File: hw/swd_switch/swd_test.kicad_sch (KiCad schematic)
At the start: 11 parts, among them J1 SWD_IN, J2 Conn_01x04, J3 SWD_PWR, J4 SWD_OUT, U1 SN74LVC2G66, U2 SN74LVC2G66, U3 SN74LVC2G66

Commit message: Added MPNs for SWD_Switch
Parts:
- J1, J4: DKPN (none) -> 609-3695-1-ND; MPN (none) -> 20021121-00010C4LF
- U1, U2, U3: DKPN (none) -> 296-13272-1-ND; MPN (none) -> SN74LVC2G66DCUR
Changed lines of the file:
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@@
-(kicad_sch (version 20210621) (generator eeschema)
+(kicad_sch (version 20211123) (generator eeschema)
   (paper "A4")
   (title_block
     (title "Debugotron SWD Switch")
-    (date "2021-11-14")
+    (date "2022-01-16")
     (rev "1.0")
     (company "Quesadillon LLC")
   )
-  (junction (at 218.44 114.3) (diameter 0) (color 0 0 0 0))
-  (junction (at 81.28 43.18) (diameter 0) (color 0 0 0 0))
-  (junction (at 88.9 114.3) (diameter 0) (color 0 0 0 0))
-  (junction (at 88.9 38.1) (diameter 0) (color 0 0 0 0))
+  (junction (at 88.9 38.1) (diameter 0) (color 0 0 0 0)
+  )
+  (junction (at 81.28 43.18) (diameter 0) (color 0 0 0 0)
+  )
+  (junction (at 218.44 114.3) (diameter 0) (color 0 0 0 0)
+  )
+  (junction (at 88.9 114.3) (diameter 0) (color 0 0 0 0)
+  )
   (wire (pts (xy 81.28 55.88) (xy 81.28 58.42))
     (stroke (width 0) (type default) (color 0 0 0 0))
@@
     )
     (property "Datasheet" "http://infocenter.arm.com/help/topic/com.arm.doc.ddi0314h/DDI0314H_coresight_components_trm.pdf" (id 3) (at 227.33 128.27 90)
+      (effects (font (size 1.27 1.27)) hide)
+    )
+    (property "DKPN" "609-3695-1-ND" (id 4) (at 218.44 96.52 0)
+      (effects (font (size 1.27 1.27)) hide)
+    )
+    (property "MPN" "20021121-00010C4LF" (id 5) (at 218.44 96.52 0)
       (effects (font (size 1.27 1.27)) hide)
     )
@@
       (effects (font (size 1.27 1.27)) hide)
     )
+    (property "DKPN" "296-13272-1-ND" (id 4) (at 147.32 93.98 0)
+      (effects (font (size 1.27 1.27)) hide)
+    )
+    (property "MPN" "SN74LVC2G66DCUR" (id 5) (at 147.32 93.98 0)
+      (effects (font (size 1.27 1.27)) hide)
+    )
     (pin "1")
     (pin "2")
@@
     )
     (property "Datasheet" "http://infocenter.arm.com/help/topic/com.arm.doc.ddi0314h/DDI0314H_coresight_components_trm.pdf" (id 3) (at 80.01 128.27 90)
+      (effects (font (size 1.27 1.27)) hide)
+    )
+    (property "DKPN" "609-3695-1-ND" (id 4) (at 88.9 96.52 0)
+      (effects (font (size 1.27 1.27)) hide)
+    )
+    (property "MPN" "20021121-00010C4LF" (id 5) (at 88.9 96.52 0)
       (effects (font (size 1.27 1.27)) hide)
     )
@@
       (effects (font (size 1.27 1.27)) hide)
     )
+    (property "DKPN" "296-13272-1-ND" (id 4) (at 147.32 58.42 0)
+      (effects (font (size 1.27 1.27)) hide)
+    )
+    (property "MPN" "SN74LVC2G66DCUR" (id 5) (at 147.32 58.42 0)
+      (effects (font (size 1.27 1.27)) hide)
+    )
     (pin "1")
     (pin "2")
@@
       (effects (font (size 1.27 1.27)) hide)
     )
+    (property "DKPN" "296-13272-1-ND" (id 4) (at 147.32 129.54 0)
+      (effects (font (size 1.27 1.27)) hide)
+    )
+    (property "MPN" "SN74LVC2G66DCUR" (id 5) (at 147.32 129.54 0)
+      (effects (font (size 1.27 1.27)) hide)
+    )

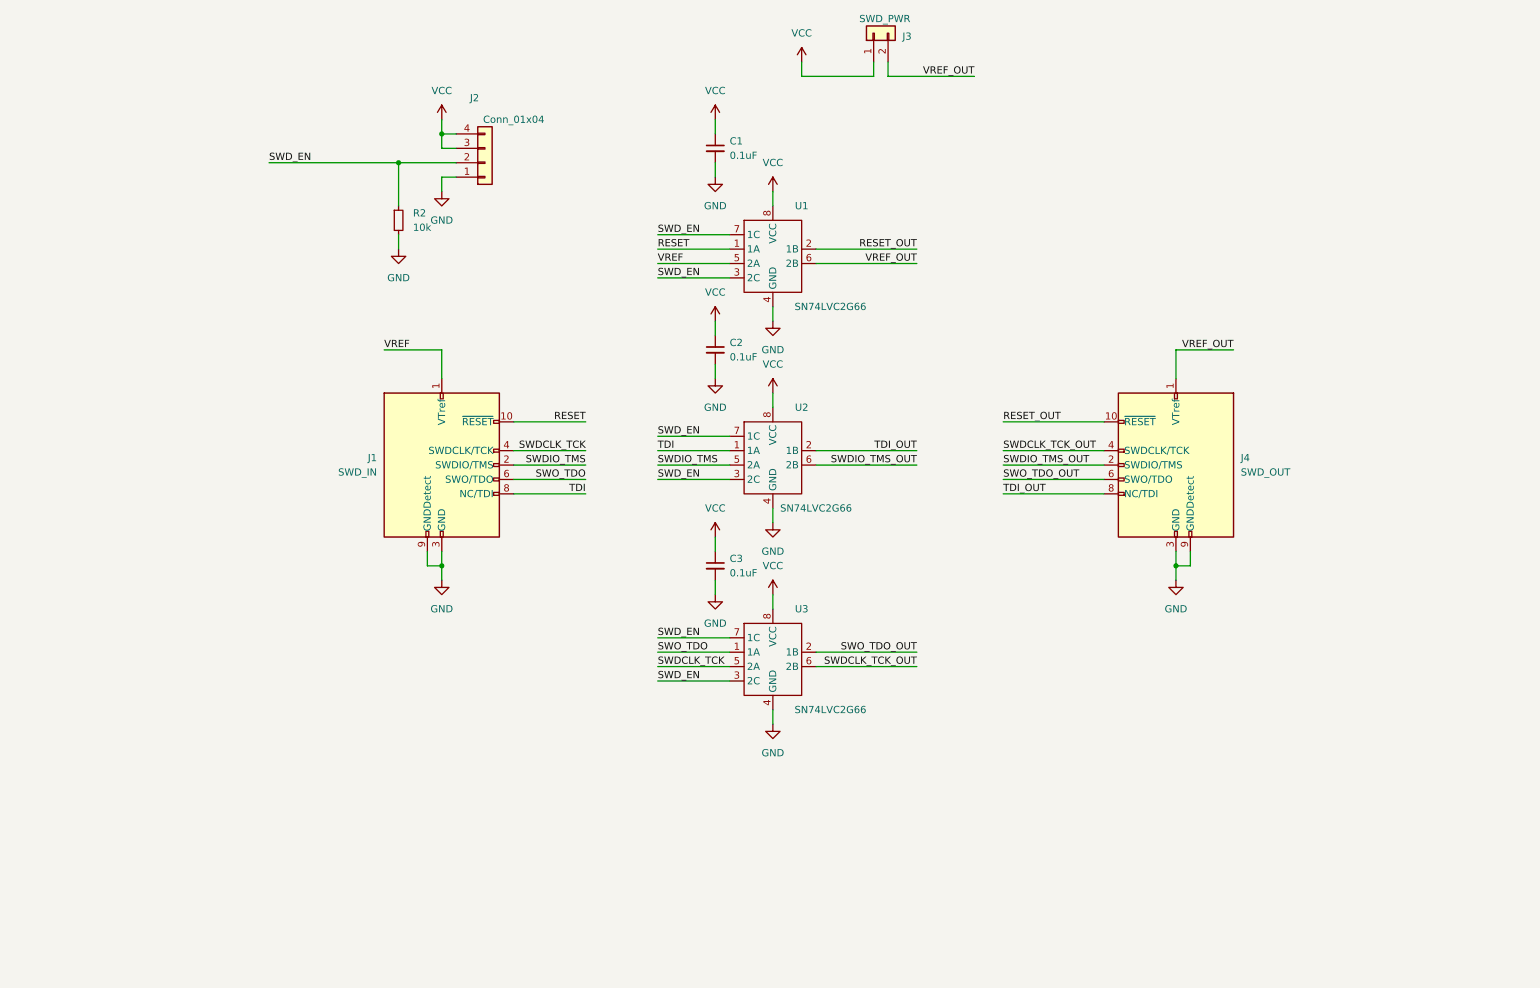
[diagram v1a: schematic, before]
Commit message: Updated debugotron v2.0 and ordered
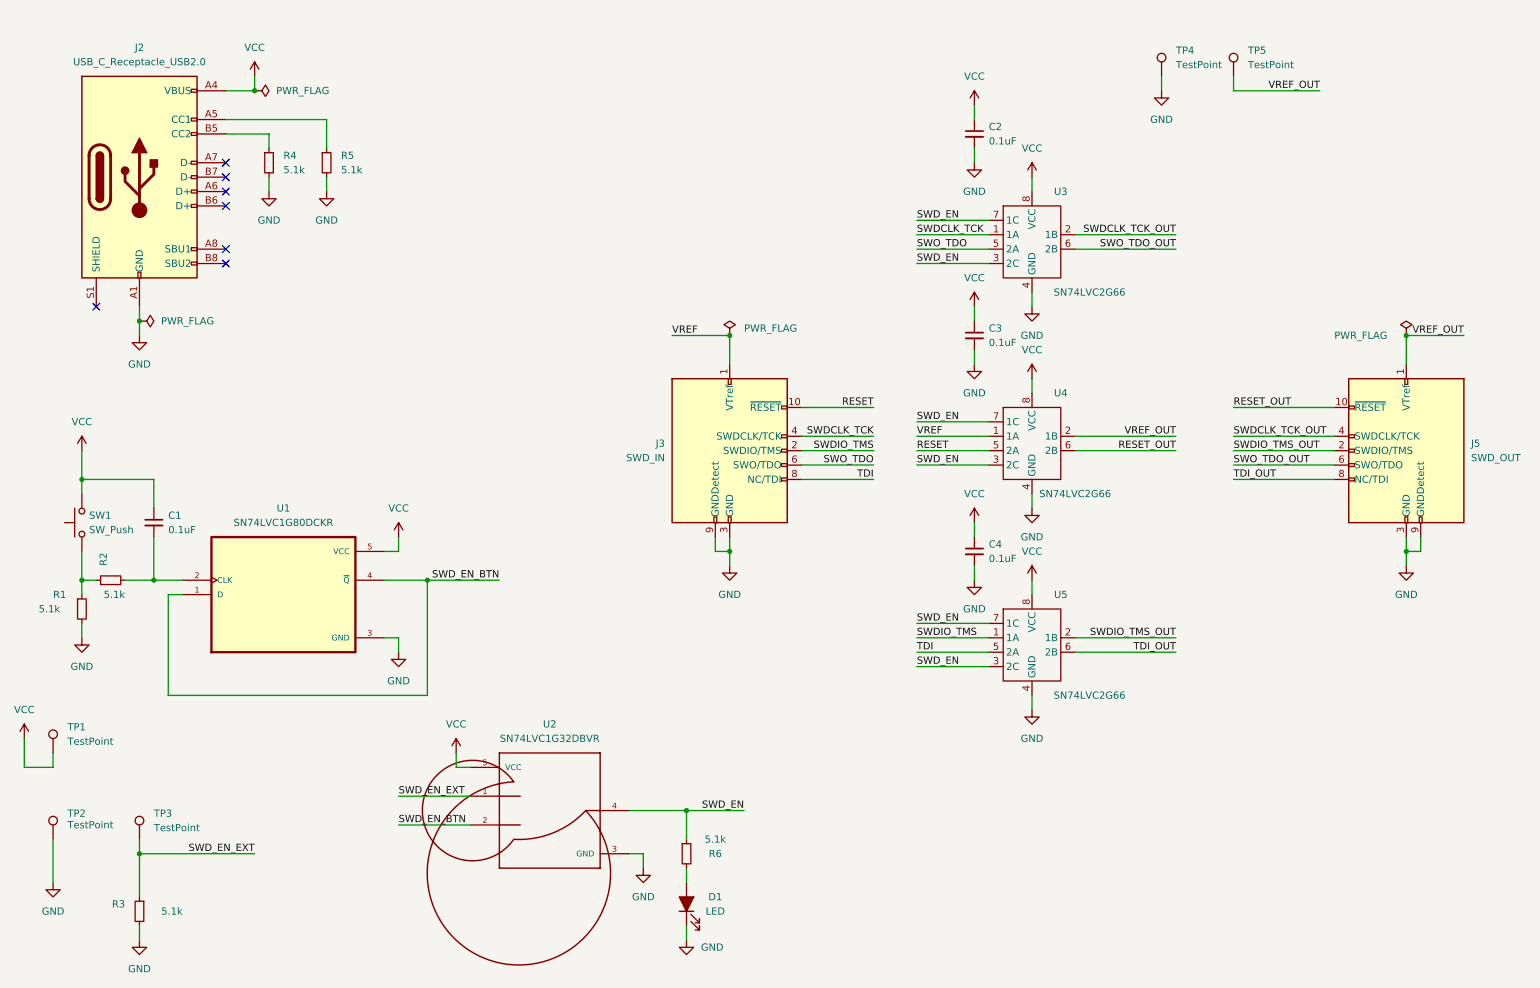
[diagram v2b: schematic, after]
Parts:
- removed J2: Conn_01x04, Connector_PinHeader_2.54mm:PinHeader_1x04_P2.54mm_Vertical, symbol Connector_Generic:Conn_01x04
- removed J3: SWD_PWR, Connector_PinHeader_2.54mm:PinHeader_1x02_P2.54mm_Vertical, symbol Connector_Generic:Conn_01x02
- added C1: 0.1uF, Capacitor_SMD:C_0402_1005Metric, symbol Device:C_Small
- added D1: LED, LED_SMD:LED_0603_1608Metric, symbol Device:LED_Filled
- added J2: USB_C_Receptacle_USB2.0, alvarop:USB4515-GF-A, symbol Connector:USB_C_Receptacle_USB2.0
- added R1, R2, R4, R5, R6: 5.1k, Resistor_SMD:R_0402_1005Metric, symbol Device:R_Small
- added SW1: SW_Push, alvarop:PTS636_G, symbol Switch:SW_Push
- added TP1, TP2, TP3, TP4, TP5: TestPoint, TestPoint:TestPoint_Pad_D3.0mm, symbol Connector:TestPoint
- added U1: SN74LVC1G80DCKR, snapeda:SOT65P210X110-5N, symbol snapeda:SN74LVC1G80DCKR
- added U2: SN74LVC1G32DBVR, snapeda:SOT95P280X145-5N, symbol snapeda:SN74LVC1G32DBVR
- J3: renamed from J1; footprint Connector_PinHeader_1.27mm:PinHeader_2x05_P1.27mm_Vertical_SMD -> snapeda:SAMTEC_FTSH-105-01-F-DV-P-TR_alt
- J5: renamed from J4; footprint Connector_PinHeader_1.27mm:PinHeader_2x05_P1.27mm_Vertical_SMD -> snapeda:SAMTEC_FTSH-105-01-F-DV-P-TR_alt
- R3: renamed from R2; value 10k -> 5.1k
- U3: renamed from U1; footprint alvaro:SN74LVC2G66-VSSOP -> alvarop:SN74LVC2G66-VSSOP
- U4: renamed from U2; footprint alvaro:SN74LVC2G66-VSSOP -> alvarop:SN74LVC2G66-VSSOP
- U5: renamed from U3; footprint alvaro:SN74LVC2G66-VSSOP -> alvarop:SN74LVC2G66-VSSOP
- renumbered C1 to C2, C2 to C3, C3 to C4
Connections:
- net GND: now also D1.1 (K), J2.A1 (GND), J2.A12 (GND), J2.B1 (GND), J2.B12 (GND), R1.2, R4.2, R5.2, TP2.1, TP4.1, U1.3 (GND), U2.3 (GND)
- net RESET: now also U4.5 (2A); no longer U3.1 (1A)
- net RESET_OUT: now also U4.6 (2B); no longer U3.2 (1B)
- net SWDCLK_TCK: now also U3.1 (1A); no longer U5.5 (2A)
- net SWDCLK_TCK_OUT: now also U3.2 (1B); no longer U5.6 (2B)
- net SWDIO_TMS: now also U5.1 (1A); no longer U4.5 (2A)
- net SWDIO_TMS_OUT: now also U5.2 (1B); no longer U4.6 (2B)
- net SWD_EN: now also R6.1, U2.4; no longer R3.1
- net SWO_TDO: now also U3.5 (2A); no longer U5.1 (1A)
- net SWO_TDO_OUT: now also U3.6 (2B); no longer U5.2 (1B)
- net TDI: now also U5.5 (2A); no longer U4.1 (1A)
- net TDI_OUT: now also U5.6 (2B); no longer U4.2 (1B)
- net VCC: now also C1.1, J2.A4 (VBUS), J2.A9 (VBUS), J2.B4 (VBUS), J2.B9 (VBUS), SW1.2, TP1.1, U1.5 (VCC), U2.5 (VCC)
- net VREF: now also U4.1 (1A); no longer U3.5 (2A)
- net VREF_OUT: now also U4.2 (1B), TP5.1; no longer U3.6 (2B)
- new net: R1.1, R2.1, SW1.1
- new net: D1.2 (A), R6.2
- new net: C1.2, R2.2, U1.2 (CLK)
- new net: J2.A5 (CC1), R5.1
- new net: J2.B5 (CC2), R4.1
- new net SWD_EN_BTN: U1.1 (D), U1.4 (~{Q}), U2.2
- new net SWD_EN_EXT: R3.1, TP3.1, U2.1
- no-connect marks 0 -> 7
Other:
- moved on the sheet: C2, C3, C4, J3, J5, R3, U3, U4, U5

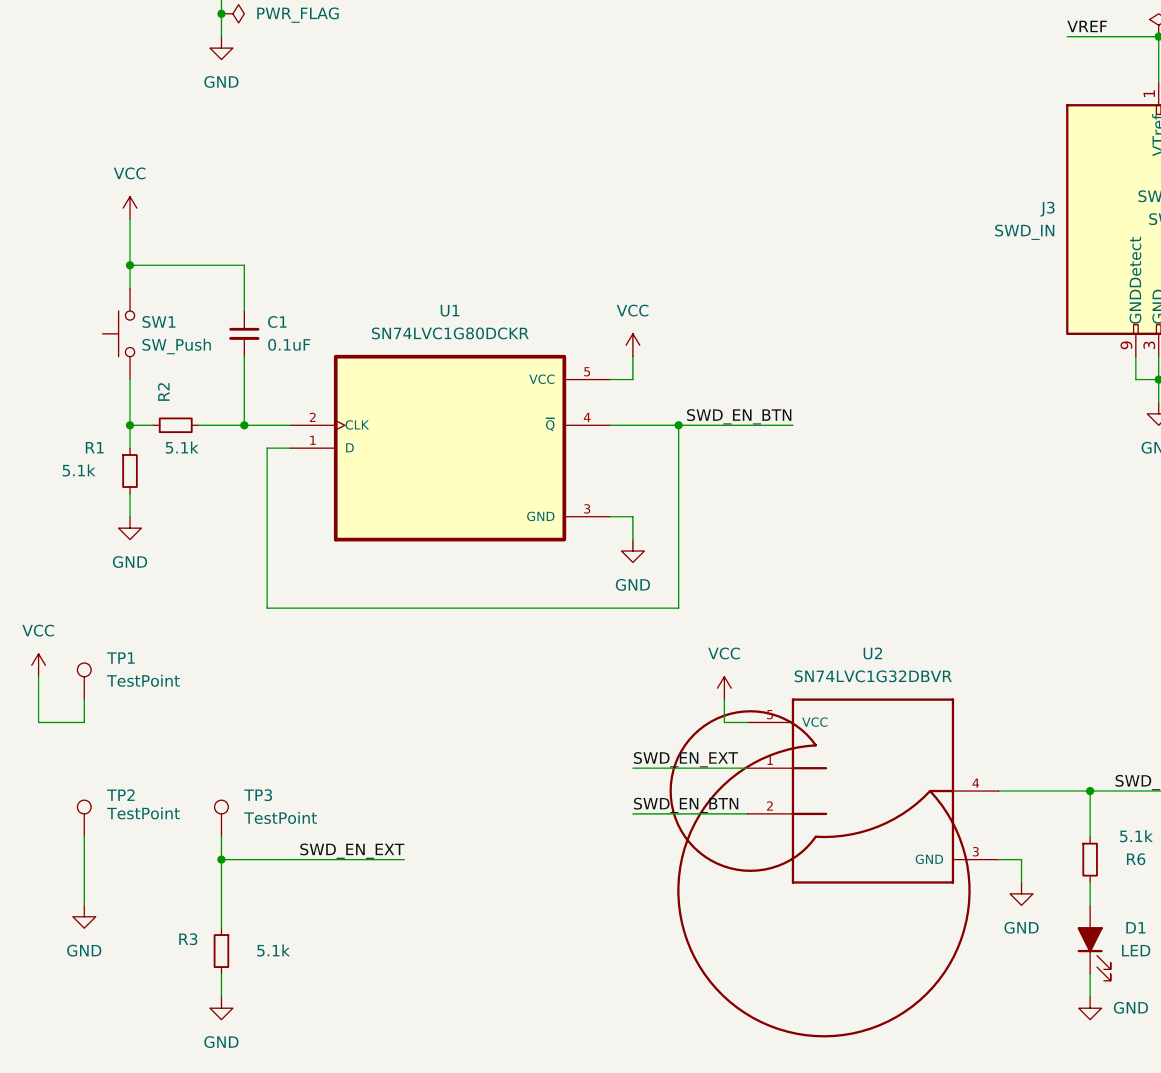
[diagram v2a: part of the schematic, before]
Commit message: Updated SWD switch to 2.1
Added schmitt trigger buffer to debounce circuit
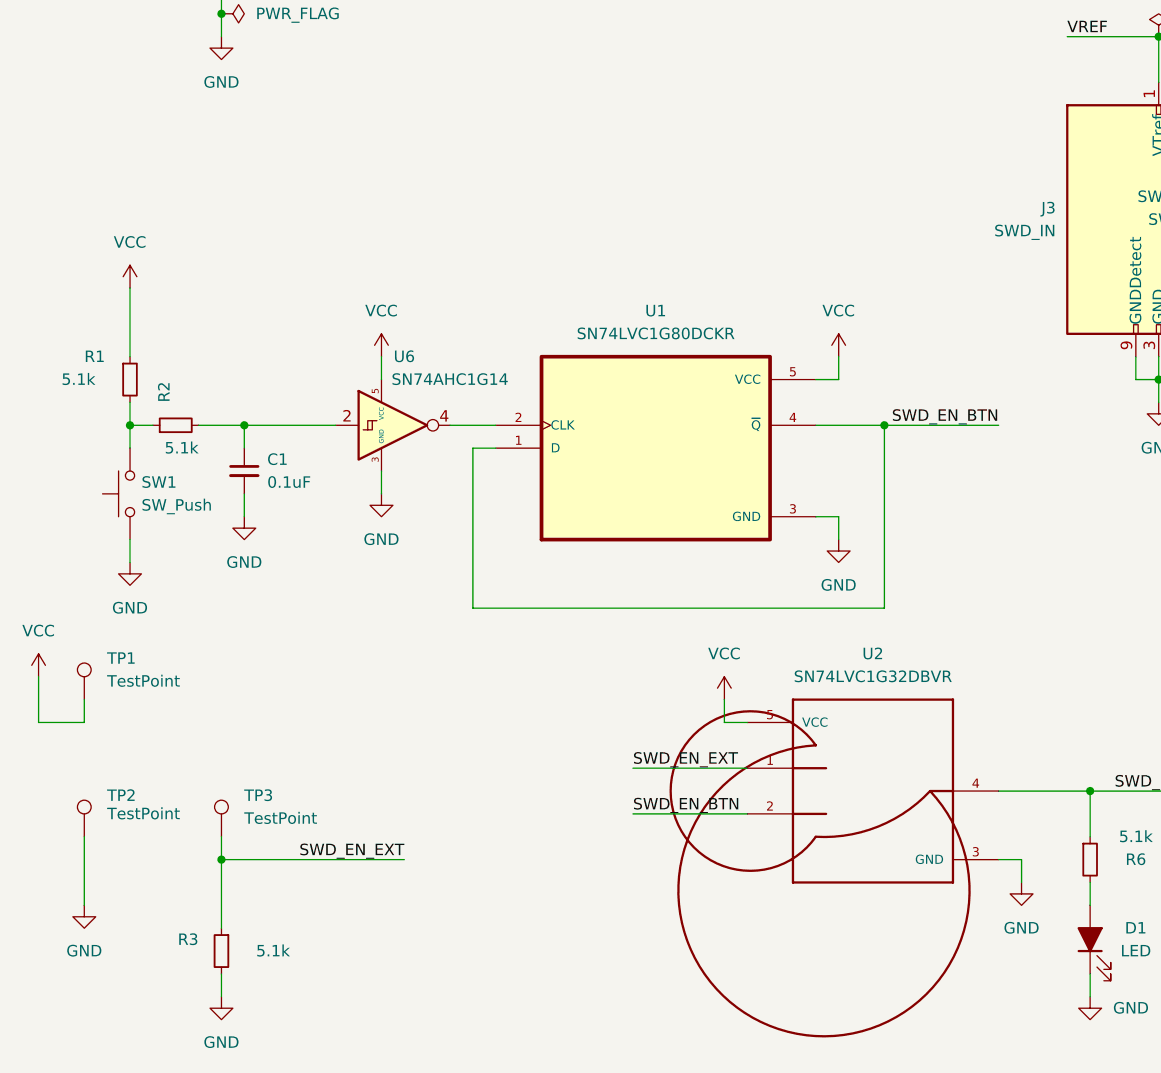
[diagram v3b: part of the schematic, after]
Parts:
- added U6: SN74AHC1G14, Package_TO_SOT_SMD:SOT-23-5, symbol 74xGxx:SN74LVC1G14DBV
- J2: MPN (none) -> USB4515-GF-A
- SW1: MPN (none) -> PTS636SL43SMTRLFS
- U1: MPN (none) -> SN74LVC1G80DCKR
- U2: MANUFACTURER Texas Instruments -> (none); MAXIMUM_PACKAGE_HEIGHT 1.45mm -> (none); MPN (none) -> SN74AHC1G32DBVR
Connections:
- net GND: now also C1.2, SW1.1, U6.3 (GND); no longer R1.2
- net VCC: now also R1.1, U6.5 (VCC); no longer C1.1, SW1.2
- new net: R1.2, R2.1, SW1.2
- new net: U1.2 (CLK), U6.4
- new net: C1.1, R2.2, U6.2
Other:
- moved on the sheet: C1, R1, SW1, U1
